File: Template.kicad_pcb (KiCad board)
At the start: 2 copper layers, 62 x 62 mm, 154 parts, among them J10 TAG, J20 TAG, J50 Goldpin, J60 RS232_Power, J61 RS232_Data, J70 USB, J84 Key, J86 Key, J87 Key, J90 12VIN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

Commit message: Testowa modyfikacja
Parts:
- removed BT90: BATTERY, Pin_Headers:Pin_Header_Straight_1x02_Pitch2.54mm
- removed C10, C11, C12, C20, C23, C30, C50, C60, C61, C62, C63, C64, C70, C73, C74, C83, C94: 100n, _obudowy:C_0603
- removed C13, C14, C40: 15p, _obudowy:C_0603
- removed C21, C24: 1u, _obudowy:C_0603
- removed C22, C25, C93, C95: 10u, _obudowy:C_0603
- removed C71, C72: 22p, _obudowy:C_0603
- removed C90: 10u/50V, Capacitors_SMD:CP_Elec_5x5.8
- removed C91: 100n/50V, _obudowy:C_0603
- removed C92: 10n, _obudowy:C_0603
- removed D801, D802, D803, D804: Red, _obudowy:LED_0805
- removed D811, D812, D813, D814: Green, _obudowy:LED_0805
- removed D821, D822, D823, D824: Blue, _obudowy:LED_0805
- removed D84, D90, D91, D93, D94: SS14, _obudowy:D_SMA_DO214AC
- removed D92: 1N4148, _obudowy:D_0805
- removed G***: LOGO, _obudowy:SafliLogo
- removed J10, J20: TAG, _obudowy:TAG-TC2050
- removed J50: Goldpin, Pin_Headers:Pin_Header_Straight_2x05_Pitch1.27mm_SMD
- removed J60: RS232_Power, _obudowy:ADAM_TECH_EB59A-1-02-A-R
- removed J61: RS232_Data, _obudowy:ADAM_TECH_EB59A-1-02-A-R
- removed J70: USB, Pin_Headers:Pin_Header_Straight_1x04_Pitch2.54mm
- removed J84, J86, J87: Key, _obudowy:ADAM_TECH_EB59A-1-02-A-R
- removed J90: 12VIN, _obudowy:ADAM_TECH_EB59A-1-02-A-R
- removed K85: CONFIG, _obudowy:TACT_6x3.5_SMD
- removed L10, L70: BLM18PG471SN1, _obudowy:L_0603
- removed L90: 4.7uH, _obudowy:DJNR4018-5020
- removed R30, R31, R85, R86, R87, R901, R903, R904, R905, R91: 10k, _obudowy:R_0603
- removed R70, R71: 22R, _obudowy:R_0603
- removed R72, R73, R95: 0R, _obudowy:R_0603
- removed R800, R810, R820, R83, R84: 1k, _obudowy:R_0603
- removed R801, R802, R803, R804, R811, R812, R813, R814, R821, R822, R823, R824: 220R, _obudowy:R_0805
- removed R900, R902: 100k, _obudowy:R_0603
- removed R92: 1M, _obudowy:R_0603
- removed R93: 27k, _obudowy:R_0603
- removed R94: 5k1, _obudowy:R_0603
- removed RY80: RayexR1, _obudowy:Relay-Rayex1357
- removed S83: LD-BZEL-T54-0505, _obudowy:Loudity-SMT54
- removed T80, T81, T82, T83, T84, T90: BC847, _obudowy:SOT23
- removed TP10: LinkRx, _obudowy:Testpoint_1.00mm
- removed TP11: LinkTx, _obudowy:Testpoint_1.00mm
- removed TP12, TP32, TP56, TP63, TP72: GND, _obudowy:Testpoint_1.00mm
- removed TP30: SDA, _obudowy:Testpoint_1.00mm
- removed TP31: SCL, _obudowy:Testpoint_1.00mm
- removed TP50: Reset-RFID, _obudowy:Testpoint_1.00mm
- removed TP51: CS-RFID, _obudowy:Testpoint_1.00mm
- removed TP52: CS-Flash, _obudowy:Testpoint_1.00mm
- removed TP53: MISO, _obudowy:Testpoint_1.00mm
- removed TP54: MOSI, _obudowy:Testpoint_1.00mm
- removed TP55: SCK, _obudowy:Testpoint_1.00mm
- removed TP60: Vcc, _obudowy:Testpoint_1.00mm
- removed TP61: V+, _obudowy:Testpoint_1.00mm
- removed TP62: V-, _obudowy:Testpoint_1.00mm
- removed TP70: ComRx, _obudowy:Testpoint_1.00mm
- removed TP71: ComTx, _obudowy:Testpoint_1.00mm
- removed TP90: 5V, _obudowy:Testpoint_1.00mm
- removed TP91: 3V3, _obudowy:Testpoint_1.00mm
- removed U10: ATmega4809-MFR, _obudowy:QFN-48-1EP_6x6mm_Pitch0.4mm
- removed U20: ATSAMW25-MR210PB, _obudowy:SAMW25
- removed U30: ATECC608A-SSHDA, w_smd_dil:so-8
- removed U31: ATECC608A-MAHDA, _obudowy:DFN-8-1EP_3x2mm_Pitch0.5mm
- removed U40: GD25Q64C, w_smd_dil:soij-8
- removed U60: MAX3232, w_smd_dil:so-16
- removed U70: FT230XQ, _obudowy:QFN-16-1EP_4x4mm_Pitch0.65mm
- removed U90: AP3211, _obudowy:SOT23-6
- removed U91: 1117-3.3, _obudowy:SOT223
- removed X10: 32768Hz, _obudowy:Crystal_3.2x1.5
- added D1: LED, _obudowy:LED_1206, F.Cu at (131.0, 104.0)
- added R1: R, _obudowy:R_1206, F.Cu at (127.0, 94.0)
- added T1: BC847, _obudowy:SOT23, F.Cu at (139.0, 98.0)
- ICON1, ICON2, ICON3, ICON4: moved to F.Cu
- moved SCR2 127.9 mm to (147.0, 86.0)
- moved ICON2 123.5 mm to (131.0, 84.0), turned to 0 degrees
- moved FID2 118.7 mm to (107.0, 111.0)
- moved FID5 118.7 mm to (107.0, 111.0)
- moved ICON4 106.2 mm to (138.0, 84.0), turned to 0 degrees
- moved ICON1 95.6 mm to (124.0, 84.0), turned to 0 degrees
- moved SCR1 92.8 mm to (113.0, 105.0)
- moved FID3 92.0 mm to (152.0, 111.0)
- moved FID6 92.0 mm to (152.0, 111.0)
- moved FID1 69.6 mm to (107.0, 81.0)
- moved FID4 69.6 mm to (107.0, 81.0)
- moved ICON3 55.8 mm to (117.0, 84.0), turned to 0 degrees
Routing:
- net GND: track 719.1 -> 12.2 mm, vias 193 -> 0
- net 3V3: track 297.2 -> 0.00 mm, vias 13 -> 0
- net 5V: track 218.6 -> 0.00 mm, vias 1 -> 0
- net Net-(R821-Pad1): track 157.5 -> 0.00 mm, vias 1 -> 0
- net Net-(R811-Pad1): track 153.3 -> 0.00 mm, vias 1 -> 0
- net Net-(R801-Pad1): track 148.6 -> 0.00 mm, vias 1 -> 0
- net /AVR/Com-Tx: track 73.9 -> 0.00 mm, vias 2 -> 0
- net /AVR/Com-Rx: track 70.6 -> 0.00 mm, vias 4 -> 0
- net Net-(J84-Pad2): track 66.6 -> 0.00 mm
- net /AVR/Key-Config: track 64.5 -> 0.00 mm, vias 3 -> 0
- net /AVR/Volt-BAT: track 51.0 -> 0.00 mm, vias 4 -> 0
- net /AVR/I2C-SDA: track 49.7 -> 0.00 mm, vias 2 -> 0
- net /AVR/Volt-DC: track 49.3 -> 0.00 mm, vias 4 -> 0
- net /AVR/I2C-SCL: track 48.1 -> 0.00 mm, vias 2 -> 0
- net /AVR/SAM-Reset: track 46.3 -> 0.00 mm, vias 1 -> 0
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- removed copper zone on B.Cu, net GND
- removed copper zone on F.Cu, net GND
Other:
- board size 62 x 62 mm -> 51 x 36 mm
- board text removed: "-IN+"
- board text removed: "-OUT+"
- board text removed: "0"
- board text removed: "11"
- board text removed: "15"
- board text removed: "20"
- board text removed: "3"
- board text removed: "4"
- board text removed: "47"
- board text removed: "49"
- board text removed: "53"
- board text removed: "58"
- board text removed: "59"
- board text removed: "62"
- board text removed: "9"
- board text removed: "BOT"
- board text removed: "Halko v100"
- board text removed: "K-In"
- board text removed: "K-Out"
- board text removed: "Relay"
- board text removed: "SAFLI"
- board text removed: "TOP"
- board text removed: "Tx Rx"

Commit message: Testowa zmiana schematu i plytki
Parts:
- added J1: Z, _obudowy:TACT_3x2.4_SMD, F.Cu at (124.0, 105.0)
- added R2: R, _obudowy:R_1206, F.Cu at (122.0, 94.0)
- moved D1 4.47 mm to (135.0, 106.0)
- moved R1 4.47 mm to (131.0, 96.0)
- moved T1 4.47 mm to (143.0, 100.0)
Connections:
- D1 pad 2: (no net) -> 5V
- R1 pad 1: GND -> Net-(J1-Pad1)
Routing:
- net GND: track 12.2 -> 72.8 mm
- net Net-(J1-Pad1): track 0.00 -> 21.0 mm
- net 5V: track 0.00 -> 11.0 mm
- net Net-(R1-Pad2): track 16.0 -> 16.5 mm
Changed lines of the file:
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@@
 (kicad_pcb (version 4) (host pcbnew 4.0.7)
   (general
-    (links 5)
-    (no_connects 2)
+    (links 10)
+    (no_connects 0)
     (area 103.924999 77.924999 155.075001 114.075001)
     (thickness 1.6)
     (drawings 4)
-    (tracks 9)
+    (tracks 31)
     (zones 0)
-    (modules 15)
-    (nets 4)
+    (modules 17)
+    (nets 6)
   )
   (page A4)
@@
   )
   (setup
-    (last_trace_width 0.4)
+    (last_trace_width 0.2)
     (user_trace_width 0.15)
     (user_trace_width 0.2)
@@
   (net 2 "Net-(D1-Pad1)")
   (net 3 "Net-(R1-Pad2)")
+  (net 4 5V)
+  (net 5 "Net-(J1-Pad1)")
   (net_class Default "To jest domyślna klasa połączeń."
     (clearance 0.15)
@@
     (uvia_dia 0.3)
     (uvia_drill 0.1)
+    (add_net 5V)
     (add_net "Net-(D1-Pad1)")
+    (add_net "Net-(J1-Pad1)")
     (add_net "Net-(R1-Pad2)")
   )
@@
   )
   (module _obudowy:LED_1206 (layer F.Cu)
-    (at 131 104 180)
+    (at 135 106 180)
     (descr "Diode SMD 1206, reflow soldering http://datasheets.avx.com/schottky.pdf")
     (tags "Diode 1206")
@@
     (pad 1 smd rect (at -1.5 0 180) (size 1 1.8) (layers F.Cu F.Paste F.Mask)
       (net 2 "Net-(D1-Pad1)"))
-    (pad 2 smd rect (at 1.5 0 180) (size 1 1.8) (layers F.Cu F.Paste F.Mask))
+    (pad 2 smd rect (at 1.5 0 180) (size 1 1.8) (layers F.Cu F.Paste F.Mask)
+      (net 4 5V))
     (model ${KISYS3DMOD}/LEDs.3dshapes/LED_1206.wrl
       (at (xyz 0 0 0))
@@
   )
   (module _obudowy:R_1206 (layer F.Cu)
-    (at 127 94 90)
+    (at 131 96 90)
     (descr "Resistor SMD 1206, reflow soldering, Vishay (see dcrcw.pdf)")
     (tags "resistor 1206")
@@
     (fp_line (start 2.15 1.1) (end -2.15 1.1) (layer F.CrtYd) (width 0.05))
     (pad 1 smd rect (at -1.5 0 90) (size 1 1.8) (layers F.Cu F.Paste F.Mask)
-      (net 1 GND))
+      (net 5 "Net-(J1-Pad1)"))
     (pad 2 smd rect (at 1.5 0 90) (size 1 1.8) (layers F.Cu F.Paste F.Mask)
       (net 3 "Net-(R1-Pad2)"))
@@
   )
   (module _obudowy:SOT23 (layer F.Cu)
-    (at 139 98 180)
+    (at 143 100 180)
     (descr SOT23)
     (fp_text reference T1 (at -2.2 0 270) (layer F.SilkS)
@@
     (pad "" thru_hole circle (at 1.166726 -1.166726) (size 0.6 0.6) (drill 0.4) (layers *.Cu *.Mask))
   )
+  (module _obudowy:TACT_3x2.4_SMD (layer F.Cu)
+    (at 124 105 180)
+    (descr "SMD Pushbutton 2")
+    (autoplace_cost180 10)
+    (fp_text reference J1 (at 0 -2 180) (layer F.SilkS)
+      (effects (font (size 0.6 0.6) (thickness 0.15)))
+    )
+    (fp_text value Z (at 0 2 180) (layer F.SilkS)
+      (effects (font (size 0.6 0.6) (thickness 0.15)))
+    )
+    (fp_line (start -1.5 -1.2) (end -1.7 -1.2) (layer F.SilkS) (width 0.1))
+    (fp_line (start -1.7 -1.2) (end -1.7 -0.7) (layer F.SilkS) (width 0.1))
+    (fp_line (start -1.7 -0.7) (end -1.5 -0.7) (layer F.SilkS) (width 0.1))
+    (fp_line (start -1.5 1.2) (end -1.7 1.2) (layer F.SilkS) (width 0.1))
+    (fp_line (start -1.7 1.2) (end -1.7 0.7) (layer F.SilkS) (width 0.1))
+    (fp_line (start -1.7 0.7) (end -1.5 0.7) (layer F.SilkS) (width 0.1))
+    (fp_line (start 1.5 1.2) (end 1.7 1.2) (layer F.SilkS) (width 0.1))
+    (fp_line (start 1.7 1.2) (end 1.7 0.7) (layer F.SilkS) (width 0.1))
+    (fp_line (start 1.7 0.7) (end 1.5 0.7) (layer F.SilkS) (width 0.1))
+    (fp_line (start 1.5 -1.2) (end 1.7 -1.2) (layer F.SilkS) (width 0.1))
+    (fp_line (start 1.7 -1.2) (end 1.7 -0.7) (layer F.SilkS) (width 0.1))
+    (fp_line (start 1.7 -0.7) (end 1.5 -0.7) (layer F.SilkS) (width 0.1))
+    (fp_line (start 1.5 1.3) (end 1.5 -1.3) (layer F.SilkS) (width 0.1))
+    (fp_line (start -1.5 -1.3) (end -1.5 1.3) (layer F.SilkS) (width 0.1))
+    (fp_circle (center 0 0) (end 0.5 0) (layer F.SilkS) (width 0.1))
+    (fp_line (start -1.5 -1.3) (end 1.5 -1.3) (layer F.SilkS) (width 0.1))
+    (fp_line (start 1.5 1.3) (end -1.5 1.3) (layer F.SilkS) (width 0.1))
+    (pad 2 smd rect (at -1.5 -0.95 180) (size 0.8 0.7) (layers F.Cu F.Paste F.Mask)
+      (net 4 5V))
+    (pad 1 smd rect (at 1.5 0.95 180) (size 0.8 0.7) (layers F.Cu F.Paste F.Mask)
+      (net 5 "Net-(J1-Pad1)"))
+    (pad 1 smd rect (at -1.5 0.95 180) (size 0.8 0.7) (layers F.Cu F.Paste F.Mask)
+      (net 5 "Net-(J1-Pad1)"))
+    (pad 2 smd rect (at 1.5 -0.95 180) (size 0.8 0.7) (layers F.Cu F.Paste F.Mask)
+      (net 4 5V))
+    (model walter/switch/smd_push2.wrl
+      (at (xyz 0 0 0))
+      (scale (xyz 0.5 0.5 0.5))
+      (rotate (xyz 0 0 0))
+    )
+  )
+  (module _obudowy:R_1206 (layer F.Cu)
+    (at 122 94 180)
+    (descr "Resistor SMD 1206, reflow soldering, Vishay (see dcrcw.pdf)")
+    (tags "resistor 1206")
+    (attr smd)
+    (fp_text reference R2 (at 0 -1.85 180) (layer F.SilkS)
+      (effects (font (size 1 1) (thickness 0.15)))
+    )
+    (fp_text value R (at 0 0 180) (layer F.Adhes)
+      (effects (font (size 0.5 0.5) (thickness 0.075)))
+    )
+    (fp_line (start -1.2 -0.8) (end -1.2 0.8) (layer F.Fab) (width 0.1))
+    (fp_line (start 1.2 -0.8) (end 1.2 0.8) (layer F.Fab) (width 0.1))
+    (fp_line (start 1.6 -0.8) (end -1.6 -0.8) (layer F.SilkS) (width 0.1))
+    (fp_line (start -1.6 -0.8) (end -1.6 0.8) (layer F.SilkS) (width 0.1))
+    (fp_line (start -1.6 0.8) (end 1.6 0.8) (layer F.SilkS) (width 0.1))
+    (fp_line (start 1.6 0.8) (end 1.6 -0.8) (layer F.SilkS) (width 0.1))
+    (fp_line (start -1.6 0.8) (end -1.6 -0.8) (layer F.Fab) (width 0.1))
+    (fp_line (start 1.6 0.8) (end -1.6 0.8) (layer F.Fab) (width 0.1))
+    (fp_line (start 1.6 -0.8) (end 1.6 0.8) (layer F.Fab) (width 0.1))
+    (fp_line (start -1.6 -0.8) (end 1.6 -0.8) (layer F.Fab) (width 0.1))
+    (fp_line (start -2.15 -1.11) (end 2.15 -1.11) (layer F.CrtYd) (width 0.05))
+    (fp_line (start -2.15 -1.11) (end -2.15 1.1) (layer F.CrtYd) (width 0.05))
+    (fp_line (start 2.15 1.1) (end 2.15 -1.11) (layer F.CrtYd) (width 0.05))
+    (fp_line (start 2.15 1.1) (end -2.15 1.1) (layer F.CrtYd) (width 0.05))
+    (pad 1 smd rect (at -1.5 0 180) (size 1 1.8) (layers F.Cu F.Paste F.Mask)
+      (net 5 "Net-(J1-Pad1)"))
+    (pad 2 smd rect (at 1.5 0 180) (size 1 1.8) (layers F.Cu F.Paste F.Mask)
+      (net 1 GND))
+    (model ${KISYS3DMOD}/Resistors_SMD.3dshapes/R_1206.wrl
+      (at (xyz 0 0 0))
+      (scale (xyz 1 1 1))
+      (rotate (xyz 0 0 0))
+    )
+  )
   (gr_line (start 104 78) (end 104 114) (angle 90) (layer Edge.Cuts) (width 0.15))
   (gr_line (start 155 78) (end 104 78) (angle 90) (layer Edge.Cuts) (width 0.15))
   (gr_line (start 155 114) (end 155 78) (angle 90) (layer Edge.Cuts) (width 0.15))
   (gr_line (start 104 114) (end 155 114) (angle 90) (layer Edge.Cuts) (width 0.15))
-  (segment (start 127 95.5) (end 137.5 95.5) (width 0.4) (layer F.Cu) (net 1))
-  (segment (start 138.0475 96.0475) (end 138.0475 96.94336) (width 0.4) (layer F.Cu) (net 1))
-  (segment (start 137.5 95.5) (end 138.0475 96.0475) (width 0.4) (layer F.Cu) (net 1))
-  (segment (start 132.5 104) (end 137 104) (width 0.2) (layer F.Cu) (net 2))
-  (segment (start 139 102) (end 139 99.05664) (width 0.2) (layer F.Cu) (net 2))
-  (segment (start 137 104) (end 139 102) (width 0.2) (layer F.Cu) (net 2))
-  (segment (start 139.9525 96.94336) (end 139.9525 94.9525) (width 0.2) (layer F.Cu) (net 3))
-  (segment (start 137.5 92.5) (end 127 92.5) (width 0.2) (layer F.Cu) (net 3))
-  (segment (start 139.9525 94.9525) (end 137.5 92.5) (width 0.2) (layer F.Cu) (net 3))
+  (segment (start 120.5 94) (end 120.5 92) (width 0.4) (layer F.Cu) (net 1) (status 400000))
+  (segment (start 120.5 92) (end 120 92) (width 0.4) (layer F.Cu) (net 1))
+  (segment (start 121 92) (end 120 92) (width 0.4) (layer F.Cu) (net 1))
+  (segment (start 120 92) (end 116 92) (width 0.4) (layer F.Cu) (net 1))
+  (segment (start 113 95) (end 113 97) (width 0.4) (layer F.Cu) (net 1))
+  (segment (start 116 92) (end 113 95) (width 0.4) (layer F.Cu) (net 1))
+  (segment (start 127 92) (end 127 94) (width 0.4) (layer F.Cu) (net 1))
+  (segment (start 127 94) (end 129 96) (width 0.4) (layer F.Cu) (net 1))
+  (segment (start 125 92) (end 127 92) (width 0.4) (layer F.Cu) (net 1))
+  (segment (start 127 92) (end 145 92) (width 0.4) (layer F.Cu) (net 1))
+  (segment (start 147 90) (end 147 86) (width 0.4) (layer F.Cu) (net 1) (status 800000))
+  (segment (start 145 92) (end 147 90) (width 0.4) (layer F.Cu) (net 1))
+  (segment (start 113 105) (end 113 97) (width 0.4) (layer F.Cu) (net 1) (status 400000))
+  (segment (start 142.0475 98.94336) (end 142.0475 97.0475) (width 0.4) (layer F.Cu) (net 1) (status 400000))
+  (segment (start 142.0475 97.0475) (end 141 96) (width 0.4) (layer F.Cu) (net 1))
+  (segment (start 141 96) (end 129 96) (width 0.4) (layer F.Cu) (net 1))
+  (segment (start 125 92) (end 121 92) (width 0.4) (layer F.Cu) (net 1))
+  (segment (start 136.5 106) (end 141 106) (width 0.2) (layer F.Cu) (net 2))
+  (segment (start 143 104) (end 143 101.05664) (width 0.2) (layer F.Cu) (net 2))
+  (segment (start 141 106) (end 143 104) (width 0.2) (layer F.Cu) (net 2))
+  (segment (start 131 94.5) (end 142.5 94.5) (width 0.2) (layer F.Cu) (net 3) (status 400000))
+  (segment (start 143.9525 95.9525) (end 143.9525 98.94336) (width 0.2) (layer F.Cu) (net 3) (status 800000))
+  (segment (start 142.5 94.5) (end 143.9525 95.9525) (width 0.2) (layer F.Cu) (net 3))
+  (segment (start 125.5 105.95) (end 133.45 105.95) (width 0.2) (layer F.Cu) (net 4) (status C00000))
+  (segment (start 133.45 105.95) (end 133.5 106) (width 0.2) (layer F.Cu) (net 4) (status C00000))
+  (segment (start 122.5 105.95) (end 125.5 105.95) (width 0.2) (layer F.Cu) (net 4) (status C00000))
+  (segment (start 125.5 104.05) (end 122.5 104.05) (width 0.2) (layer F.Cu) (net 5) (status C00000))
+  (segment (start 123.5 97.5) (end 131 97.5) (width 0.2) (layer F.Cu) (net 5) (status 800000))
+  (segment (start 122.5 104.05) (end 122.5 98.5) (width 0.2) (layer F.Cu) (net 5) (status 400000))
+  (segment (start 123.5 97.5) (end 123.5 94) (width 0.2) (layer F.Cu) (net 5))
+  (segment (start 122.5 98.5) (end 123.5 97.5) (width 0.2) (layer F.Cu) (net 5))
 )

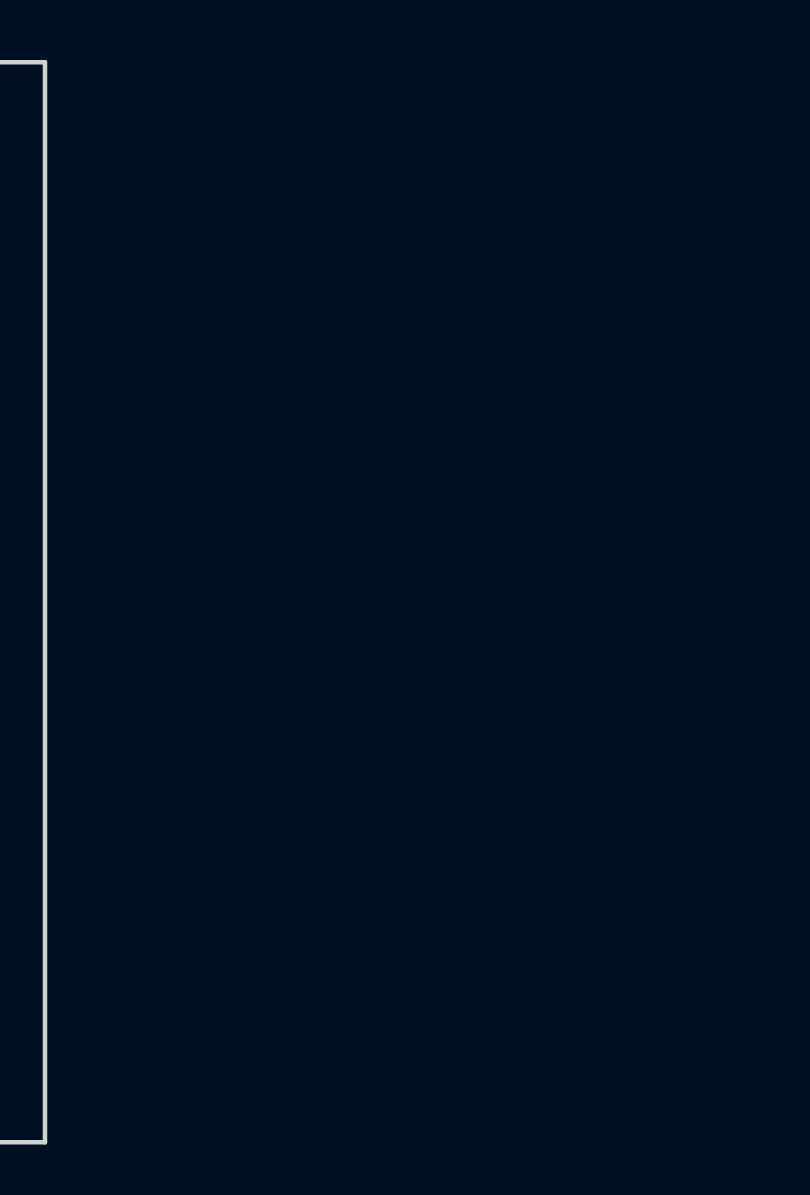
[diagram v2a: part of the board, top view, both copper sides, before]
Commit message: Added ESP32-WROOM
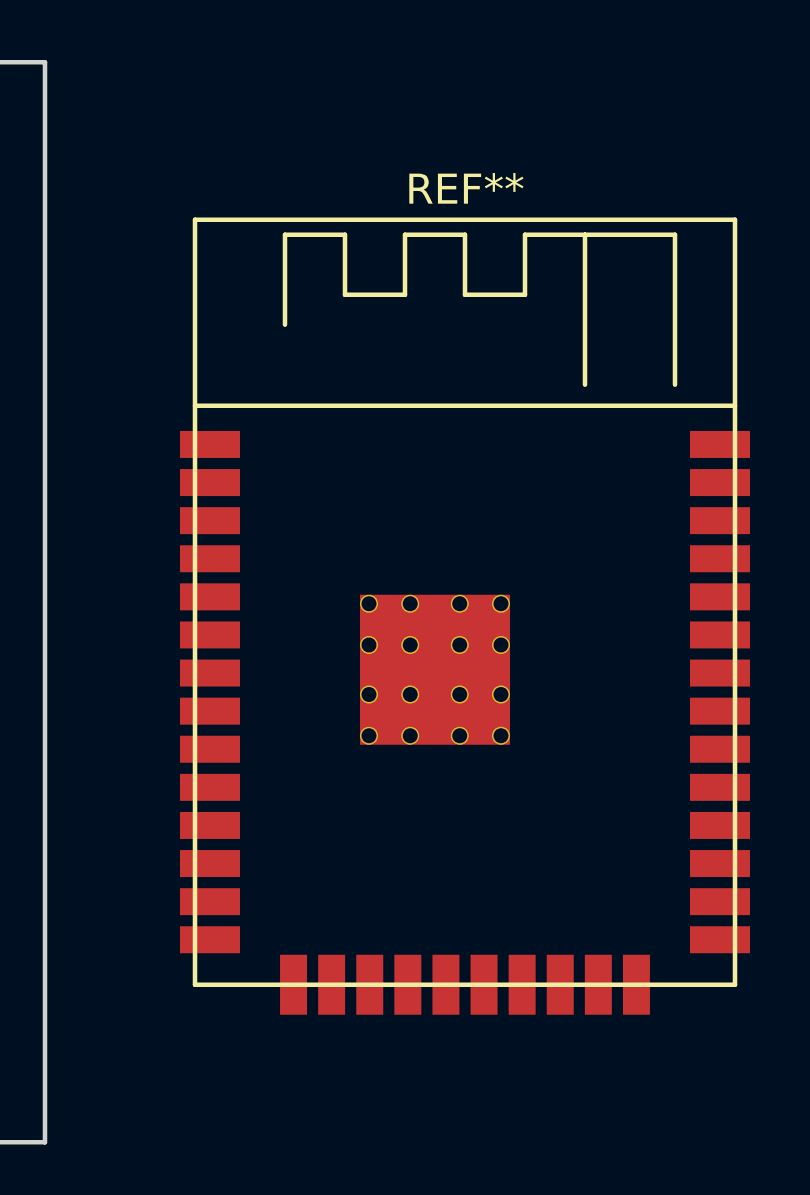
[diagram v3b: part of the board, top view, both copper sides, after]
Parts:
- added REF**: ESP32-WROOM-32E, _obudowy:ESP32-WROOM-32E, F.Cu at (169.0, 96.0)
